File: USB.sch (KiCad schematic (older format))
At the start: 8 parts

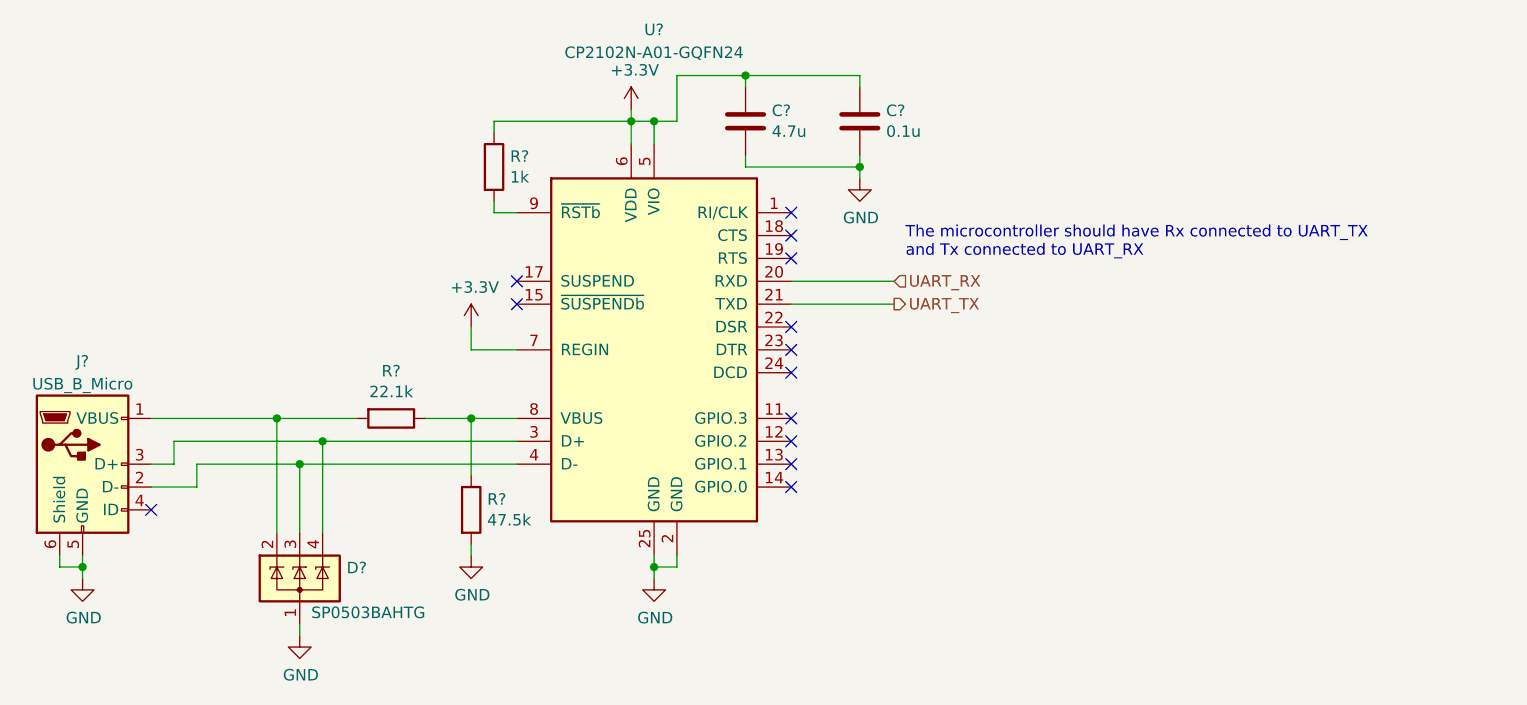
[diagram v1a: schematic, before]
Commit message: Initial layout of the Telemtry board.
The ethernet interface needs more work.
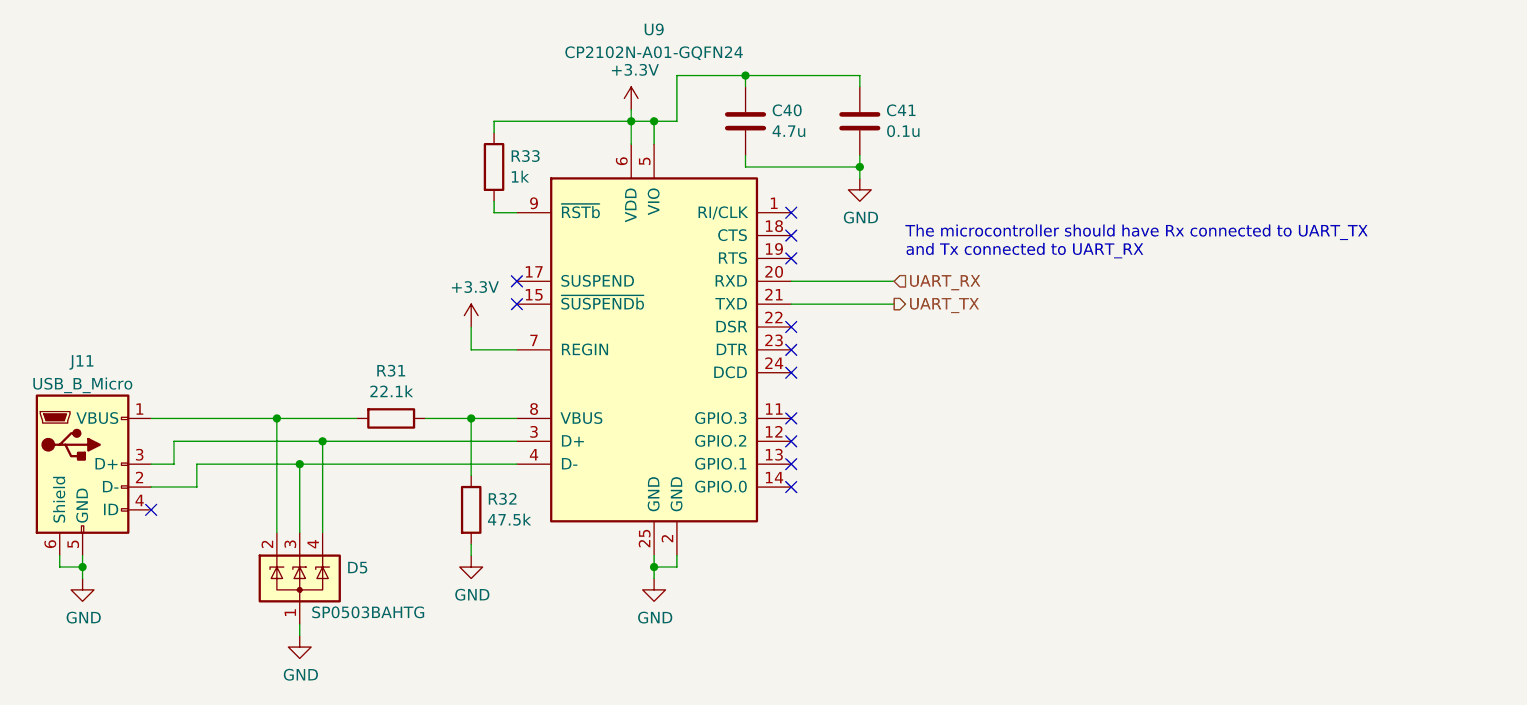
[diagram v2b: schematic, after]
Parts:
- gave numbers to parts that had none: 8
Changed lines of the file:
@@
 $EndDescr
 $Comp
-L Interface_USB:CP2102N-A01-GQFN24 U?
+L Interface_USB:CP2102N-A01-GQFN24 U9
 U 1 1 5C4963B2
 P 5500 3800
-F 0 "U?" H 5500 5200 50  0000 C CNN
+F 0 "U9" H 5500 5200 50  0000 C CNN
 F 1 "CP2102N-A01-GQFN24" H 5500 5100 50  0000 C CNN
 F 2 "Package_DFN_QFN:QFN-24-1EP_4x4mm_P0.5mm_EP2.6x2.6mm" H 5950 3000 50  0001 L CNN
@@
 $EndComp
 $Comp
-L Connector:USB_B_Micro J?
+L Connector:USB_B_Micro J11
 U 1 1 5C4964BB
 P 3000 4300
-F 0 "J?" H 3000 4750 50  0000 C CNN
+F 0 "J11" H 3000 4750 50  0000 C CNN
 F 1 "USB_B_Micro" H 3000 4650 50  0000 C CNN
 F 2 "Connector_USB:USB_Micro-B_Molex-105017-0001" H 3150 4250 50  0001 C CNN
@@
 	3500 4400 3500 4300
 $Comp
-L power:GND #PWR?
+L power:GND #PWR0166
 U 1 1 5C4965DF
 P 3000 4800
-F 0 "#PWR?" H 3000 4550 50  0001 C CNN
+F 0 "#PWR0166" H 3000 4550 50  0001 C CNN
 F 1 "GND" H 3005 4627 50  0000 C CNN
 F 2 "" H 3000 4800 50  0001 C CNN
@@
 Connection ~ 3000 4750
 $Comp
-L power:GND #PWR?
+L power:GND #PWR0167
 U 1 1 5C4966CF
 P 5500 4800
-F 0 "#PWR?" H 5500 4550 50  0001 C CNN
+F 0 "#PWR0167" H 5500 4550 50  0001 C CNN
 F 1 "GND" H 5505 4627 50  0000 C CNN
 F 2 "" H 5500 4800 50  0001 C CNN
@@
 	5500 4750 5500 4800
 $Comp
-L Power_Protection:SP0503BAHT D?
+L Power_Protection:SP0503BAHT D5
 U 1 1 5C496C9B
 P 3950 4800
-F 0 "D?" H 4155 4846 50  0000 L CNN
+F 0 "D5" H 4155 4846 50  0000 L CNN
 F 1 "SP0503BAHTG" H 4000 4650 50  0000 L CNN
 F 2 "Package_TO_SOT_SMD:SOT-143" H 4175 4750 50  0001 L CNN
@@
 $EndComp
 $Comp
-L power:GND #PWR?
+L power:GND #PWR0168
 U 1 1 5C497074
 P 3950 5050
-F 0 "#PWR?" H 3950 4800 50  0001 C CNN
+F 0 "#PWR0168" H 3950 4800 50  0001 C CNN
 F 1 "GND" H 3955 4877 50  0000 C CNN
 F 2 "" H 3950 5050 50  0001 C CNN
@@
 	3850 4600 3850 4100
 $Comp
-L Device:R R?
+L Device:R R32
 U 1 1 5C497DB9
 P 4700 4500
-F 0 "R?" H 4770 4546 50  0000 L CNN
+F 0 "R32" H 4770 4546 50  0000 L CNN
 F 1 "47.5k" H 4770 4455 50  0000 L CNN
 F 2 "Resistor_SMD:R_0805_2012Metric" V 4630 4500 50  0001 C CNN
@@
 $EndComp
 $Comp
-L Device:R R?
+L Device:R R31
 U 1 1 5C497DDB
 P 4350 4100
-F 0 "R?" V 4143 4100 50  0000 C CNN
+F 0 "R31" V 4143 4100 50  0000 C CNN
 F 1 "22.1k" V 4234 4100 50  0000 C CNN
 F 2 "Resistor_SMD:R_0805_2012Metric" V 4280 4100 50  0001 C CNN
@@
 	4200 4100 3850 4100
 $Comp
-L power:GND #PWR?
+L power:GND #PWR0169
 U 1 1 5C498DBE
 P 4700 4700
-F 0 "#PWR?" H 4700 4450 50  0001 C CNN
+F 0 "#PWR0169" H 4700 4450 50  0001 C CNN
 F 1 "GND" H 4705 4527 50  0000 C CNN
 F 2 "" H 4700 4700 50  0001 C CNN
@@
 	4700 4700 4700 4650
 $Comp
-L power:+3.3V #PWR?
+L power:+3.3V #PWR0170
 U 1 1 5C499E7D
 P 5400 2750
-F 0 "#PWR?" H 5400 2600 50  0001 C CNN
+F 0 "#PWR0170" H 5400 2600 50  0001 C CNN
 F 1 "+3.3V" H 5415 2923 50  0000 C CNN
 F 2 "" H 5400 2750 50  0001 C CNN
@@
 Connection ~ 5400 2800
 $Comp
-L Device:R R?
+L Device:R R33
 U 1 1 5C49B01B
 P 4800 3000
-F 0 "R?" H 4870 3046 50  0000 L CNN
+F 0 "R33" H 4870 3046 50  0000 L CNN
 F 1 "1k" H 4870 2955 50  0000 L CNN
 F 2 "Resistor_SMD:R_0805_2012Metric" V 4730 3000 50  0001 C CNN
@@
 	4800 2800 5400 2800
 $Comp
-L Device:C C?
+L Device:C C40
 U 1 1 5C49CC52
 P 5900 2800
-F 0 "C?" H 6015 2846 50  0000 L CNN
+F 0 "C40" H 6015 2846 50  0000 L CNN
 F 1 "4.7u" H 6015 2755 50  0000 L CNN
 F 2 "Capacitor_SMD:C_0805_2012Metric" H 5938 2650 50  0001 C CNN
@@
 NoConn ~ 6100 4400
 $Comp
-L power:+3.3V #PWR?
+L power:+3.3V #PWR0171
 U 1 1 5C4A2CBF
 P 4700 3700
-F 0 "#PWR?" H 4700 3550 50  0001 C CNN
+F 0 "#PWR0171" H 4700 3550 50  0001 C CNN
 F 1 "+3.3V" H 4715 3873 50  0000 C CNN
 F 2 "" H 4700 3700 50  0001 C CNN
@@
 	4700 3800 4900 3800
 $Comp
-L Device:C C?
+L Device:C C41
 U 1 1 5C4A4791
 P 6400 2800
-F 0 "C?" H 6515 2846 50  0000 L CNN
+F 0 "C41" H 6515 2846 50  0000 L CNN
 F 1 "0.1u" H 6515 2755 50  0000 L CNN
 F 2 "Capacitor_SMD:C_0805_2012Metric" H 6438 2650 50  0001 C CNN
@@
 $EndComp
 $Comp
-L power:GND #PWR?
+L power:GND #PWR0172
 U 1 1 5C4A4BE4
 P 6400 3050
-F 0 "#PWR?" H 6400 2800 50  0001 C CNN
+F 0 "#PWR0172" H 6400 2800 50  0001 C CNN
 F 1 "GND" H 6405 2877 50  0000 C CNN
 F 2 "" H 6400 3050 50  0001 C CNN

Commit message: Lay out the Telemetry board.
This is the initial draft of the Telemetry board layout. A few
debugging pins changed (on the SD card) for easier routing.

There is still some uncertainty with regard to the routing of the
Ethernet traces. According to my calculations, the differential
impedence between the RX+/- traces and the TX+/- traces is around
150R, which is 50% higher than one source was recommending. I am
uncertain how to reduce this though, and I am unclear as to how
much this will affect performance, especially when the traces
cover such a short distance.
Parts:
- D5: symbol Power_Protection:SP0503BAHT -> Telemetry-Primary-rescue:SP0503BAHT-Power_Protection
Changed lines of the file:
@@
 	5500 4750 5500 4800
 $Comp
-L Power_Protection:SP0503BAHT D5
+L Telemetry-Primary-rescue:SP0503BAHT-Power_Protection D5
 U 1 1 5C496C9B
 P 3950 4800

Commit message: Fix routing near crystal.
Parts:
- J11: symbol Connector:USB_B_Micro -> Telemetry-Primary-rescue:USB_B_Micro-Connector
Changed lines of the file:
@@
 $EndComp
 $Comp
-L Connector:USB_B_Micro J11
+L Telemetry-Primary-rescue:USB_B_Micro-Connector J11
 U 1 1 5C4964BB
 P 3000 4300
+AR Path="/5C4964BB" Ref="J11"  Part="1"
+AR Path="/5F6D5B75/5C4964BB" Ref="J11"  Part="1"
 F 0 "J11" H 3000 4750 50  0000 C CNN
 F 1 "USB_B_Micro" H 3000 4650 50  0000 C CNN
@@
 F 1 "4.7u" H 6015 2755 50  0000 L CNN
 F 2 "Capacitor_SMD:C_0805_2012Metric" H 5938 2650 50  0001 C CNN
-F 3 "~" H 5900 2800 50  0001 C CNN
+F 3 "https://www.mouser.com/datasheet/2/212/KEM_C1023_X7R_AUTO_SMD-1093309.pdf" H 5900 2800 50  0001 C CNN
 	1    5900 2800
 	1    0    0    -1
@@
 F 1 "0.1u" H 6515 2755 50  0000 L CNN
 F 2 "Capacitor_SMD:C_0805_2012Metric" H 6438 2650 50  0001 C CNN
-F 3 "~" H 6400 2800 50  0001 C CNN
+F 3 "https://www.mouser.com/datasheet/2/212/KEM_C1002_X7R_SMD-1102033.pdf" H 6400 2800 50  0001 C CNN
 	1    6400 2800
 	1    0    0    -1
